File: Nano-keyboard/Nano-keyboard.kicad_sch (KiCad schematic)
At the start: 27 parts, among them U1 AMS1117, U2 ESP32-WROOM-32, U3 J5019, U5 EN12-HN22AF25, U6 EN12-HN22AF25

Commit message: Initial routing
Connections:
- net ESP_EN: now also U2.3 (EN)
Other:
- note added: "Encoders"
- note added: "Power Supply"
- note added: "Switches Matrix"
- moved on the sheet: B0, B1, B10, B2, B3, B4, B5, B6, B7, B8, B9, D1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

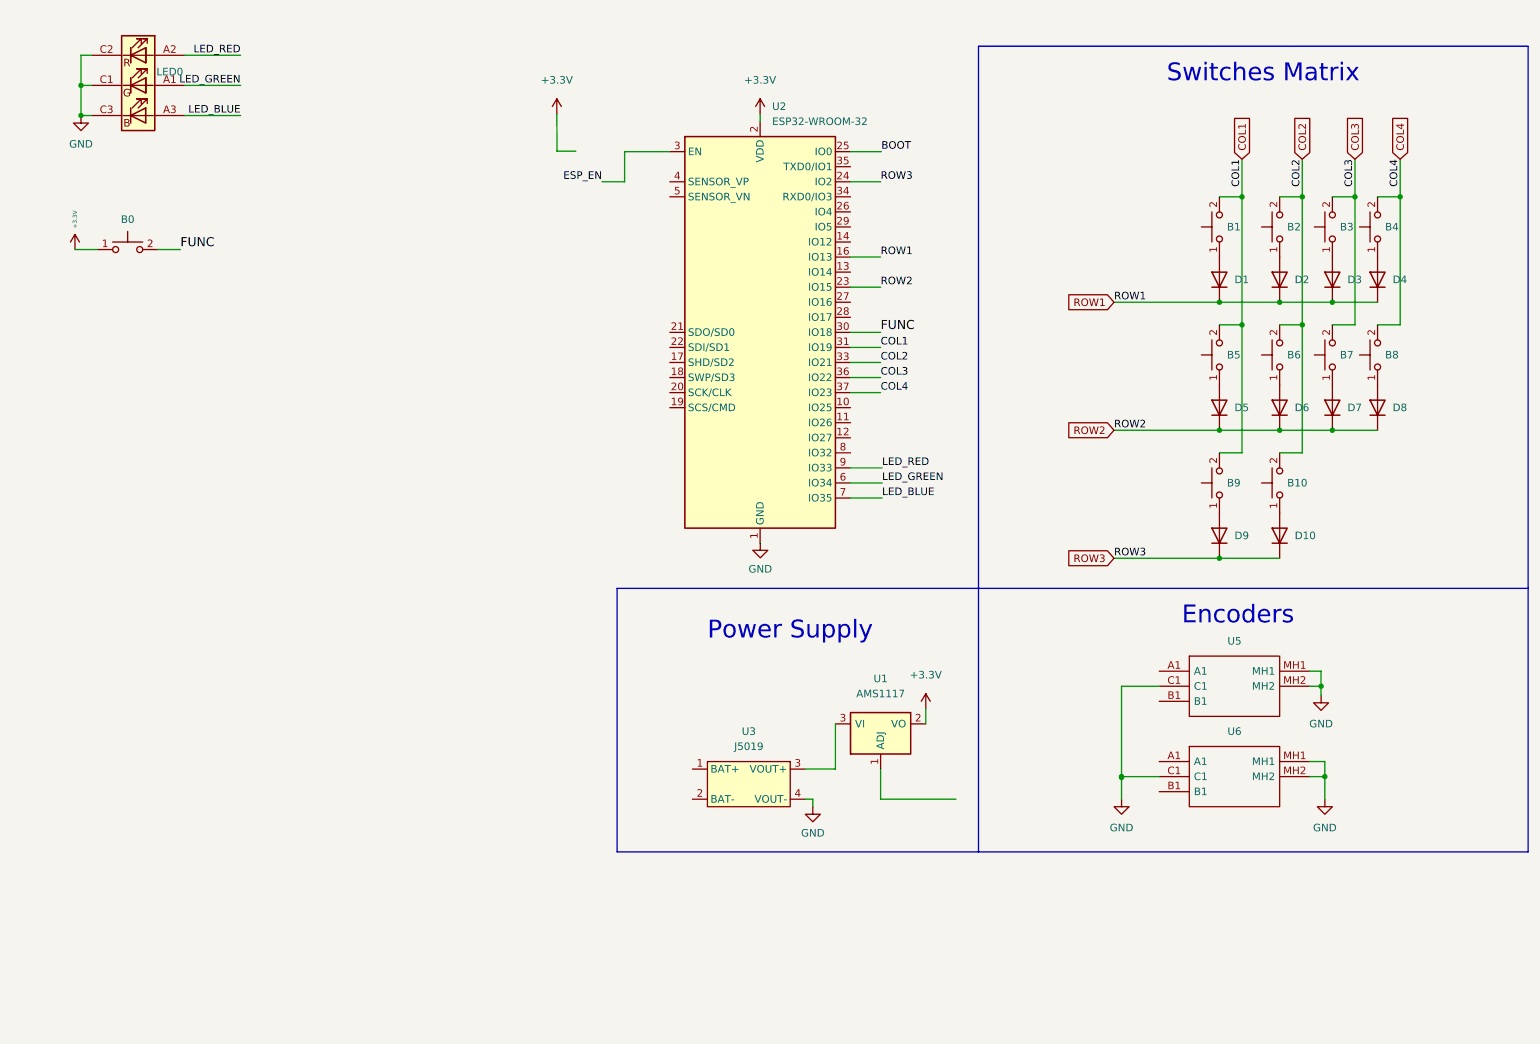
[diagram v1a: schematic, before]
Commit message: Added Resistors and Capacitor
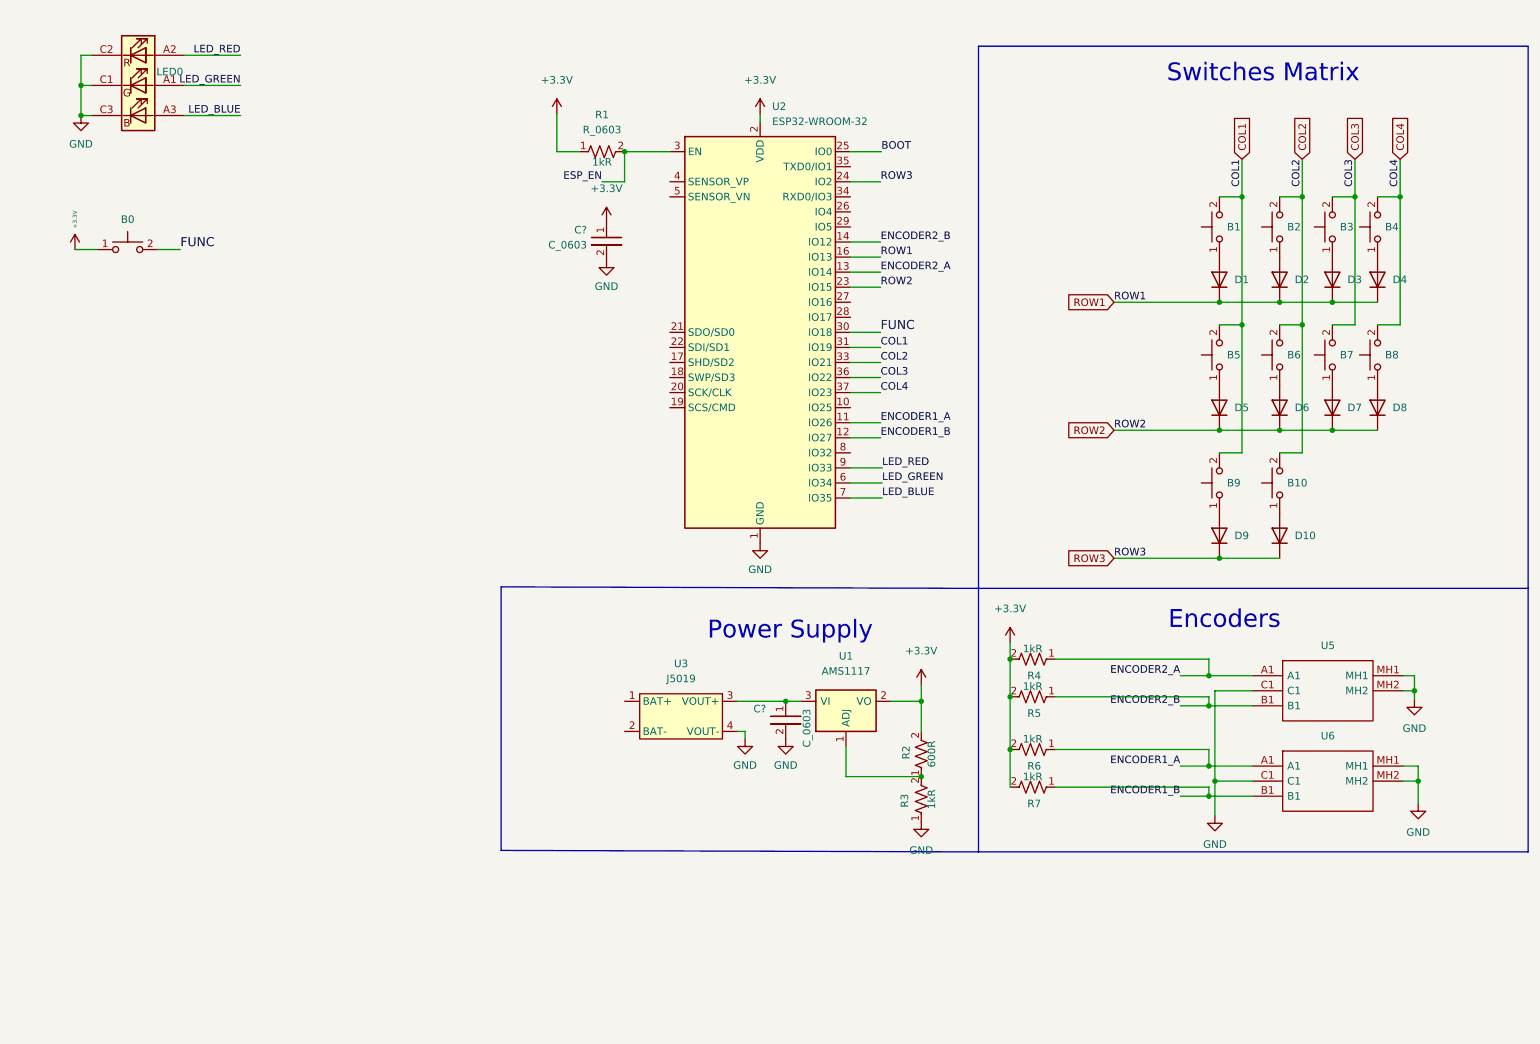
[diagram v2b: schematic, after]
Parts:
- added C? (x2): C_0603, lib:C_0603_1608Metric, symbol custom-keyboard:C_0603
- added R1, R2, R3, R4, R5, R6, R7: R_0603, lib:R_0603_1608Metric, symbol custom-keyboard:R_0603
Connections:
- net +3V3: now also C?.1, R1.1, R2.2, R4.2, R5.2, R6.2, R7.2
- net ESP_EN: now also R1.2
- net GND: now also U5.C1, U6.C1, C?.2, C?.2, R3.1
- net ENCODER1_A: now reaches U2.11 (IO26)
- net ENCODER1_A: now also U6.A1, R6.1
- net ENCODER1_B: now reaches U2.12 (IO27)
- net ENCODER1_B: now also U6.B1, R7.1
- net ENCODER2_A: now reaches U2.13 (IO14)
- net ENCODER2_A: now also U5.A1, R4.1
- net ENCODER2_B: now reaches U2.14 (IO12)
- net ENCODER2_B: now also U5.B1, R5.1
- net at U1.3 (VI), U3.3 (VOUT+): now also C?.1
- net at U1.1 (ADJ): now also R2.1, R3.2
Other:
- moved on the sheet: U1, U3, U5, U6

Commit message: Routing changes
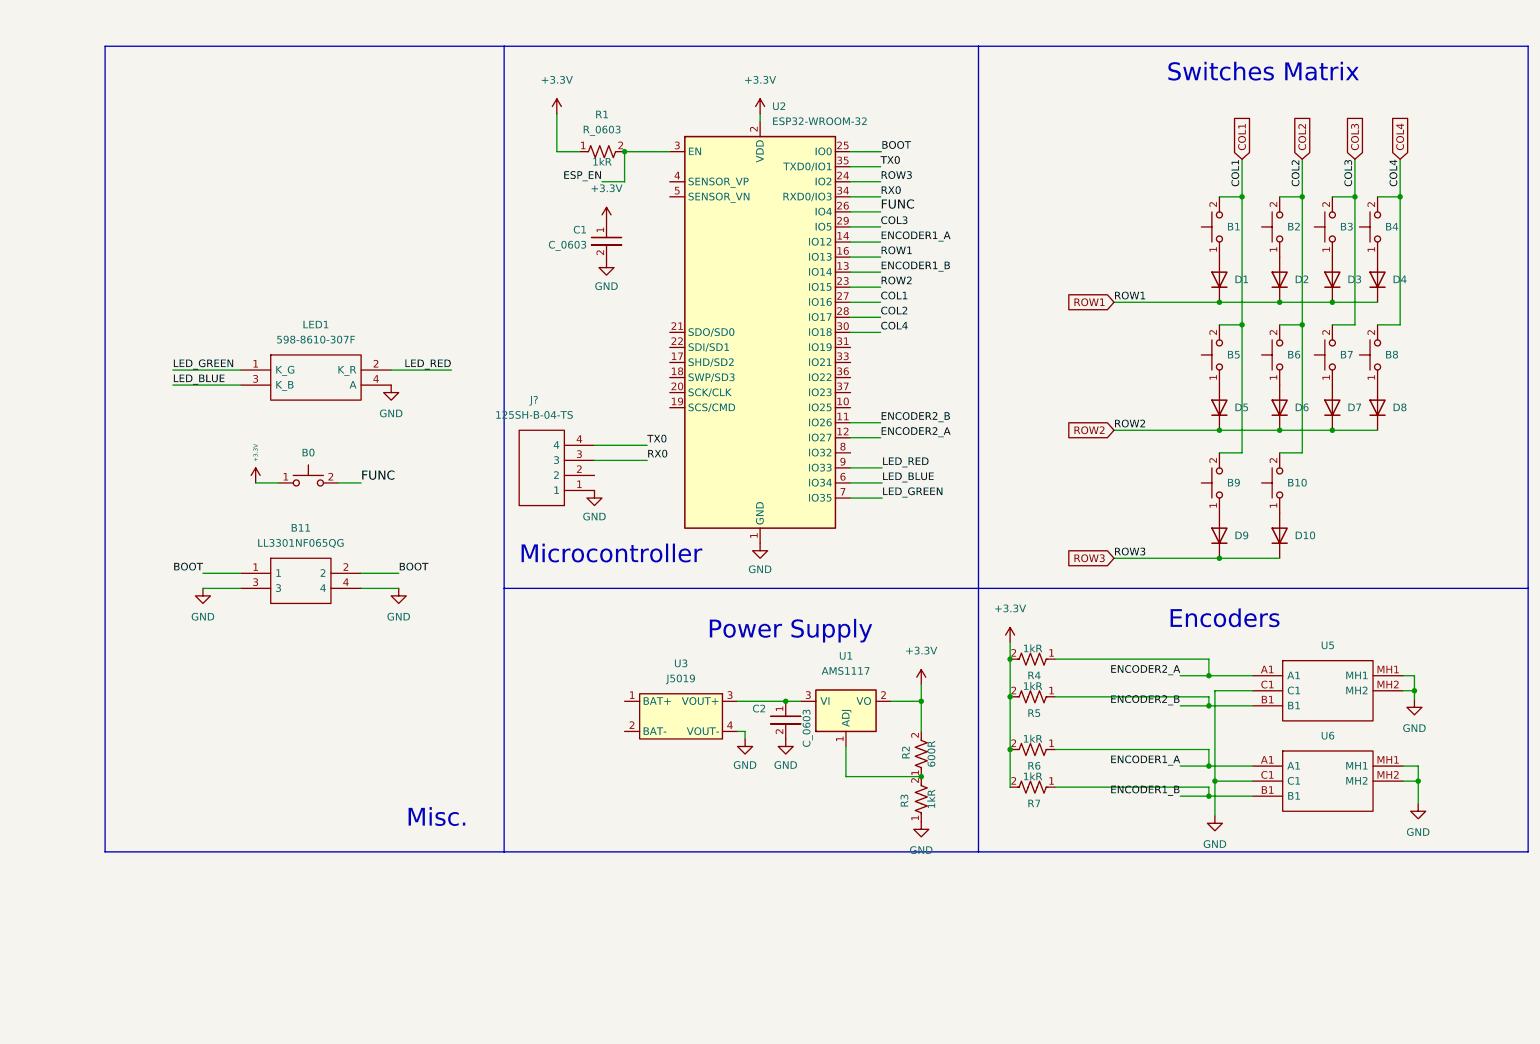
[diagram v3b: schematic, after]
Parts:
- removed LED0: LRTBGVSR-U4V2-JW+A6BB-D8+S2U2-7Z-20-S, lib:LRTBGVSRU4V2JWA6BBD8S2U27Z20S, symbol custom-keyboard:LRTBGVSR-U4V2-JW+A6BB-D8+S2U2-7Z-20-S
- added B11: LL3301NF065QG, lib:LL3301NF065QG, symbol custom-keyboard:LL3301NF065QG
- added J?: 125SH-B-04-TS, lib:SHDR4W35P0X125_1X4_800X320X420P, symbol custom-keyboard:125SH-B-04-TS
- added LED1: 598-8610-307F, lib:5988610307F, symbol custom-keyboard:598-8610-307F
- gave numbers to parts that had none: 2
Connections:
- net BOOT: now also B11.1, B11.2
- net COL1: now also U2.27 (IO16); no longer U2.31 (IO19)
- net COL2: now also U2.28 (IO17); no longer U2.33 (IO21)
- net COL3: now also U2.29 (IO5); no longer U2.36 (IO22)
- net COL4: now also U2.30 (IO18); no longer U2.37 (IO23)
- net ENCODER1_A: now also U2.14 (IO12); no longer U2.11 (IO26)
- net ENCODER1_B: now also U2.13 (IO14); no longer U2.12 (IO27)
- net ENCODER2_A: now also U2.12 (IO27); no longer U2.13 (IO14)
- net ENCODER2_B: now also U2.11 (IO26); no longer U2.14 (IO12)
- net FUNC: now also U2.26 (IO4); no longer U2.30 (IO18)
- net GND: now also B11.3, B11.4, J?.1, LED1.4 (A)
- net LED_BLUE: now also U2.6 (IO34), LED1.3 (K_B); no longer U2.7 (IO35)
- net LED_GREEN: now also U2.7 (IO35), LED1.1 (K_G); no longer U2.6 (IO34)
- net LED_RED: now also LED1.2 (K_R)
- net RX0: now reaches U2.34 (RXD0/IO3)
- net RX0: now also J?.3
- net TX0: now reaches U2.35 (TXD0/IO1)
- net TX0: now also J?.4
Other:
- note added: "Microcontroller"
- note added: "Misc."
- moved on the sheet: B0

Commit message: Updates
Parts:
- gave numbers to parts that had none: 1
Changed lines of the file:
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@@
   (symbol (lib_id "power:GND") (at 113.03 102.87 0) (unit 1)
     (in_bom yes) (on_board yes) (fields_autoplaced)
-    (property "Reference" "#PWR?" (id 0) (at 113.03 109.22 0)
+    (property "Reference" "#PWR0107" (id 0) (at 113.03 109.22 0)
       (effects (font (size 1.27 1.27)) hide)
     )
@@
   (symbol (lib_id "custom-keyboard:125SH-B-04-TS") (at 113.03 102.87 180) (unit 1)
     (in_bom yes) (on_board yes) (fields_autoplaced)
-    (property "Reference" "J?" (id 0) (at 102.87 87.63 0))
+    (property "Reference" "J1" (id 0) (at 102.87 87.63 0))
     (property "Value" "125SH-B-04-TS" (id 1) (at 102.87 90.17 0))
     (property "Footprint" "lib:SHDR4W35P0X125_1X4_800X320X420P" (id 2) (at 96.52 105.41 0)
@@
     )
     (path "/2582d951-d265-4c57-b1cd-6dfb17070961"
-      (reference "#PWR?") (unit 1) (value "GND") (footprint "")
+      (reference "#PWR0107") (unit 1) (value "GND") (footprint "")
     )
     (path "/e891b433-8f8c-451a-9a1f-eebc6bd34030"
@@
     )
     (path "/e43e3efb-457c-4631-ab67-1c5eb8150efb"
-      (reference "J?") (unit 1) (value "125SH-B-04-TS") (footprint "lib:SHDR4W35P0X125_1X4_800X320X420P")
+      (reference "J1") (unit 1) (value "125SH-B-04-TS") (footprint "lib:SHDR4W35P0X125_1X4_800X320X420P")
     )
     (path "/70c10d2e-4f0e-4847-9f68-59ba44ae2259"

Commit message: Routing Done [Pending Revision]
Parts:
- added J2: 125SH-B-02-TS, lib:125SHB02TS, symbol custom-keyboard:125SH-B-02-TS
- added R8: R_0603, lib:R_0603_1608Metric, symbol custom-keyboard:R_0603
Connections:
- net GND: now also R8.1; no longer LED1.4 (A)
- net at U3.1 (BAT+): now also J2.1
- net at U3.2 (BAT-): now also J2.2
- new net: LED1.4 (A), R8.2
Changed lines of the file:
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@@
+    (stroke (width 0) (type default) (color 0 0 0 0))
+  )
+  (wire (pts (xy 109.22 139.446) (xy 118.11 139.446))
+    (stroke (width 0) (type default) (color 0 0 0 0))
+  )
+  (wire (pts (xy 118.11 139.446) (xy 118.11 138.43))
     (stroke (width 0) (type default) (color 0 0 0 0))
   )
@@
     (stroke (width 0) (type default) (color 0 0 0 0))
   )
+  (wire (pts (xy 118.11 141.986) (xy 118.11 143.51))
+    (stroke (width 0) (type default) (color 0 0 0 0))
+  )
   (wire (pts (xy 228.6 53.34) (xy 232.41 53.34))
     (stroke (width 0) (type default) (color 0 0 0 0))
@@
   )
   (wire (pts (xy 168.148 143.51) (xy 168.148 138.43))
+    (stroke (width 0) (type default) (color 0 0 0 0))
+  )
+  (wire (pts (xy 109.22 141.986) (xy 118.11 141.986))
     (stroke (width 0) (type default) (color 0 0 0 0))
   )
@@
     (pin "2")
   )
-  (symbol (lib_id "power:GND") (at 78.74 85.09 0) (unit 1)
-    (in_bom yes) (on_board yes) (fields_autoplaced)
-    (property "Reference" "#PWR0104" (id 0) (at 78.74 91.44 0)
-      (effects (font (size 1.27 1.27)) hide)
-    )
-    (property "Value" "GND" (id 1) (at 78.74 89.916 0))
-    (property "Footprint" "" (id 2) (at 78.74 85.09 0)
-      (effects (font (size 1.27 1.27)) hide)
-    )
-    (property "Datasheet" "" (id 3) (at 78.74 85.09 0)
-      (effects (font (size 1.27 1.27)) hide)
-    )
-    (pin "1")
-  )
   (symbol (lib_id "custom-keyboard:598-8610-307F") (at 53.34 82.55 0) (unit 1)
     (in_bom yes) (on_board yes) (fields_autoplaced)
@@
     (pin "2")
   )
+  (symbol (lib_id "custom-keyboard:R_0603") (at 78.74 89.154 180) (unit 1)
+    (in_bom yes) (on_board yes)
+    (property "Reference" "R8" (id 0) (at 76.2 88.646 90))
+    (property "Value" "R_0603" (id 1) (at 75.057 88.9 90)
+      (effects (font (size 1.27 1.27)) hide)
+    )
+    (property "Footprint" "lib:R_0603_1608Metric" (id 2) (at 78.74 89.154 0)
+      (effects (font (size 1.27 1.27)) hide)
+    )
+    (property "Datasheet" "" (id 3) (at 78.74 89.154 0)
+      (effects (font (size 1.27 1.27)) hide)
+    )
+    (property "Resistance" "600R" (id 4) (at 79.756 88.9 90)
+      (effects (font (size 1.27 1.27)) (justify bottom))
+    )
+    (pin "1")
+    (pin "2")
+  )
   (symbol (lib_id "power:GND") (at 145.288 144.78 0) (unit 1)
     (in_bom yes) (on_board yes) (fields_autoplaced)
@@
     )
     (pin "1")
+  )
+  (symbol (lib_id "custom-keyboard:125SH-B-02-TS") (at 109.22 141.986 180) (unit 1)
+    (in_bom yes) (on_board yes) (fields_autoplaced)
+    (property "Reference" "J2" (id 0) (at 101.6 134.62 0))
+    (property "Value" "125SH-B-02-TS" (id 1) (at 92.71 147.066 0)
+      (effects (font (size 1.27 1.27)) (justify left) hide)
+    )
+    (property "Footprint" "lib:125SHB02TS" (id 2) (at 92.71 144.526 0)
+      (effects (font (size 1.27 1.27)) (justify left) hide)
+    )
+    (property "Datasheet" "https://datasheet.datasheetarchive.com/originals/distributors/Datasheets_SAMA/45b419e770029f3b35d1c71db0ffd901.pdf" (id 3) (at 92.71 141.986 0)
+      (effects (font (size 1.27 1.27)) (justify left) hide)
+    )
+    (property "Description" "Conn Shrouded Header HDR 2 POS 1.25mm Solder ST Top Entry Thru-Hole" (id 4) (at 92.71 139.446 0)
+      (effects (font (size 1.27 1.27)) (justify left) hide)
+    )
+    (property "Height" "4.708" (id 5) (at 92.71 136.906 0)
+      (effects (font (size 1.27 1.27)) (justify left) hide)
+    )
+    (property "Manufacturer_Name" "Adam Tech" (id 6) (at 92.71 134.366 0)
+      (effects (font (size 1.27 1.27)) (justify left) hide)
+    )
+    (property "Manufacturer_Part_Number" "125SH-B-02-TS" (id 7) (at 92.71 131.826 0)
+      (effects (font (size 1.27 1.27)) (justify left) hide)
+    )
+    (property "Mouser Part Number" "" (id 8) (at 92.71 129.286 0)
+      (effects (font (size 1.27 1.27)) (justify left) hide)
+    )
+    (property "Mouser Price/Stock" "" (id 9) (at 92.71 126.746 0)
+      (effects (font (size 1.27 1.27)) (justify left) hide)
+    )
+    (property "Arrow Part Number" "" (id 10) (at 92.71 124.206 0)
+      (effects (font (size 1.27 1.27)) (justify left) hide)
+    )
+    (property "Arrow Price/Stock" "" (id 11) (at 92.71 121.666 0)
+      (effects (font (size 1.27 1.27)) (justify left) hide)
+    )
+    (pin "1")
+    (pin "2")
   )
   (symbol (lib_id "power:GND") (at 138.43 144.78 0) (mirror y) (unit 1)
@@
     (pin "MH2")
   )
+  (symbol (lib_id "power:GND") (at 78.74 92.71 0) (unit 1)
+    (in_bom yes) (on_board yes) (fields_autoplaced)
+    (property "Reference" "#PWR0104" (id 0) (at 78.74 99.06 0)
+      (effects (font (size 1.27 1.27)) hide)
+    )
+    (property "Value" "GND" (id 1) (at 78.74 97.536 0))
+    (property "Footprint" "" (id 2) (at 78.74 92.71 0)
+      (effects (font (size 1.27 1.27)) hide)
+    )
+    (property "Datasheet" "" (id 3) (at 78.74 92.71 0)
+      (effects (font (size 1.27 1.27)) hide)
+    )
+    (pin "1")
+  )
   (symbol (lib_id "custom-keyboard:Cherry_Switch_1U_PCB") (at 228.6 80.01 90) (unit 1)
     (in_bom yes) (on_board yes) (fields_autoplaced)
@@
       (reference "#PWR0103") (unit 1) (value "+3.3V") (footprint "")
     )
-    (path "/6f542a9f-17a1-4d58-b757-d062d47cb36c"
+    (path "/ee361238-2af6-41d7-b534-e2016d0478b8"
       (reference "#PWR0104") (unit 1) (value "GND") (footprint "")
     )
@@
       (reference "J1") (unit 1) (value "125SH-B-04-TS") (footprint "lib:SHDR4W35P0X125_1X4_800X320X420P")
     )
+    (path "/c1f0ee56-9df3-45ba-8763-bac4718a84aa"
+      (reference "J2") (unit 1) (value "125SH-B-02-TS") (footprint "lib:125SHB02TS")
+    )
     (path "/70c10d2e-4f0e-4847-9f68-59ba44ae2259"
       (reference "LED1") (unit 1) (value "598-8610-307F") (footprint "lib:5988610307F")
@@
       (reference "R7") (unit 1) (value "R_0603") (footprint "lib:R_0603_1608Metric")
     )
+    (path "/94a8a32b-cb10-496b-b880-28e370d2c0b9"
+      (reference "R8") (unit 1) (value "R_0603") (footprint "lib:R_0603_1608Metric")
+    )
     (path "/f54960e4-2379-4f0c-bc91-5451a1cb3928"
